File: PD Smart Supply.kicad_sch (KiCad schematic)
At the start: 0 parts

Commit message: Added some major parts to the sheet
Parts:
- added U1: CH224A, easyeda2kicad:ESSOP-10_L4.9-W3.9-P1.0-LS6.0-TL-EP, symbol PD Smart Supply:CH224A
- added U2: TPS560430XDBVR, easyeda2kicad:SOT-23-6_L2.9-W1.6-P0.95-LS2.8-BL, symbol PD Smart Supply:TPS560430XDBVR
- added U3: STM32G071CBT6, easyeda2kicad:LQFP-48_L7.0-W7.0-P0.50-LS9.0-BL, symbol PD Smart Supply:STM32G071CBT6
- added USB1: USB4105-GF-A-060, easyeda2kicad:USB-C-SMD_GT-USB-7010E-1, symbol PD Smart Supply:USB4105-GF-A-060
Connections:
- new net: USB1.A4B9 (VBUS), USB1.B4A9 (VBUS)
- new net: U1.4 (DP), USB1.A6 (DP1), USB1.B6 (DP2)
- new net: U1.5 (DM), USB1.A7 (DN1), USB1.B7 (DN2)
- new net CC1: USB1.A5 (CC1)
- new net CC2: USB1.B5 (CC2)
- new net GND: USB1.1 (GND), USB1.2 (GND), USB1.3 (GND), USB1.4 (GND), USB1.A1B12 (GND), USB1.B1A12 (GND)
- no-connect marks 0 -> 2

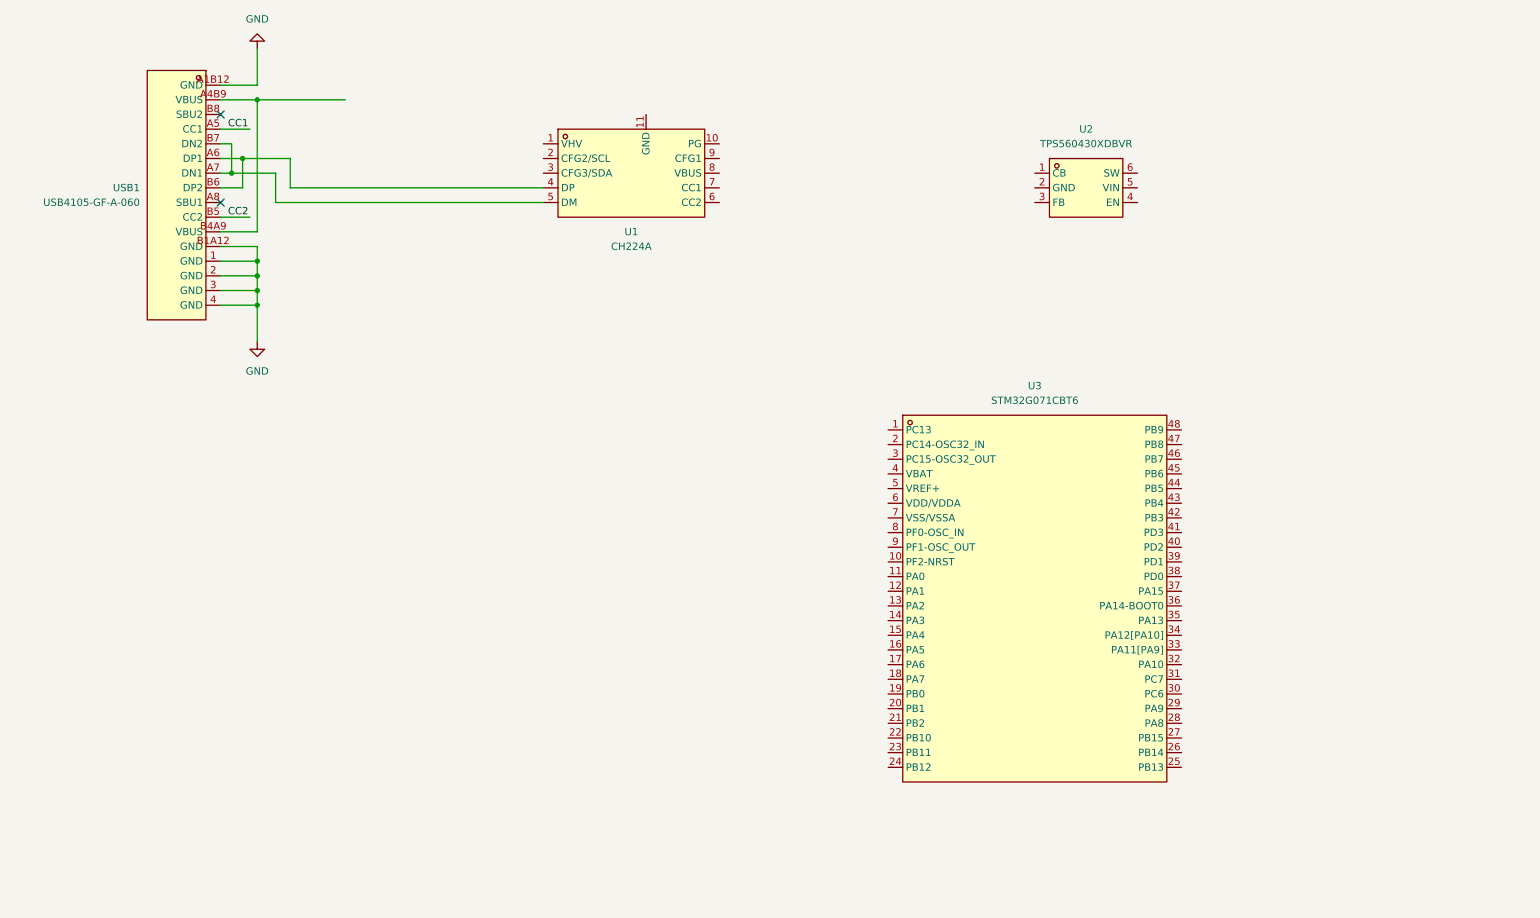
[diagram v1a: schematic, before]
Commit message: Finished schematic work for USB C, pd chip, board 3v3 regulator and added the mcu
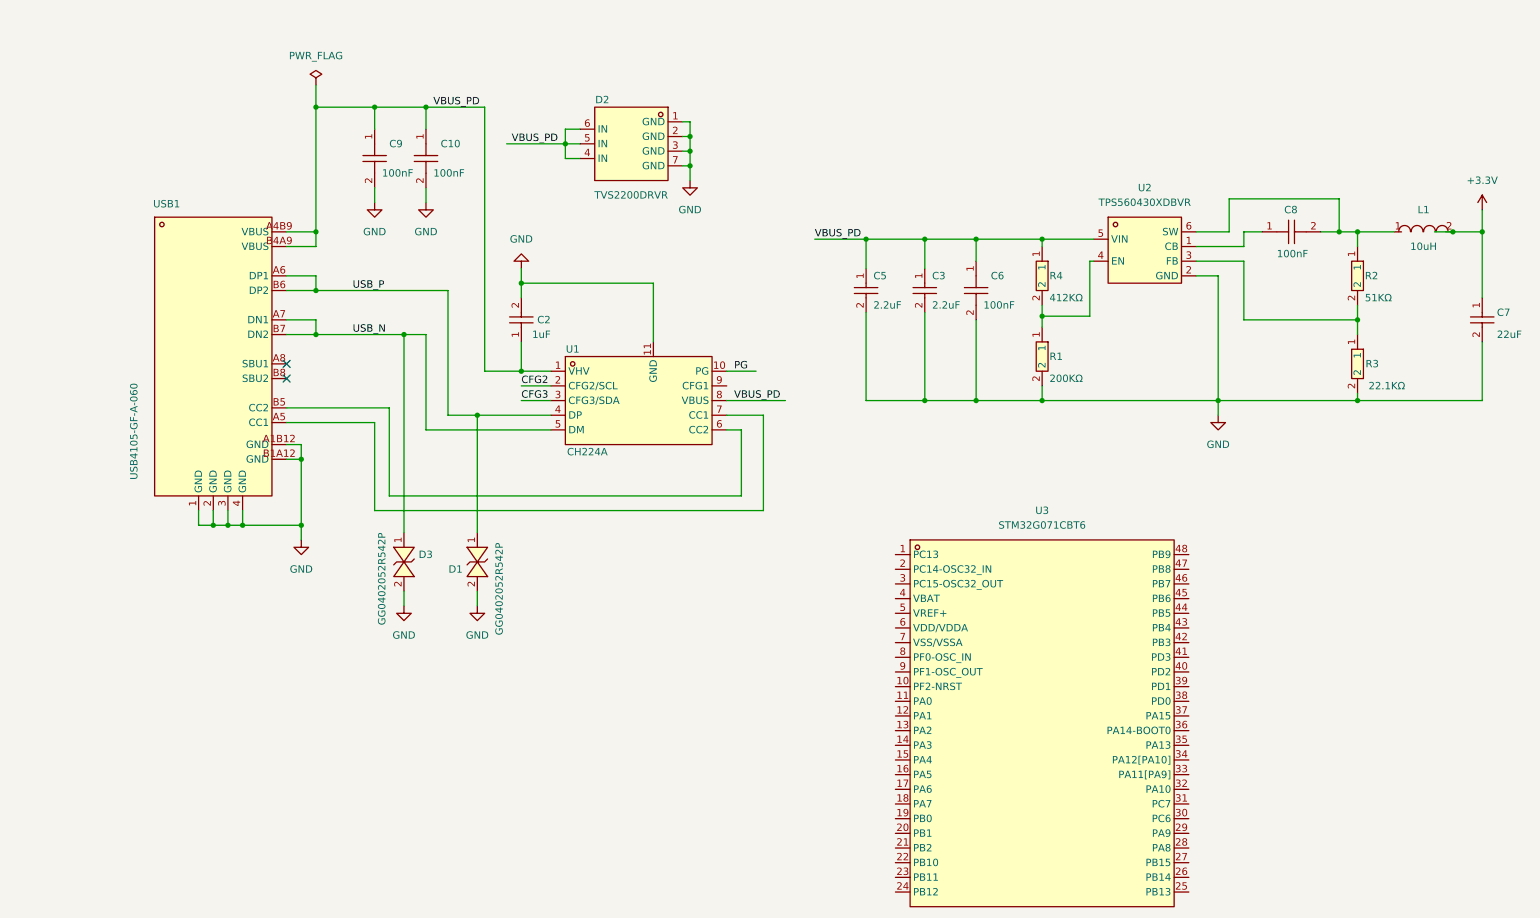
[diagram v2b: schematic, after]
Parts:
- added C10, C6, C8, C9: 100nF, easyeda2kicad:C0603, symbol PD Smart Supply:CC0603KRX7R9BB104
- added C2: 1uF, easyeda2kicad:C0805, symbol PD Smart Supply:CL21B105KBFNNNE
- added C3, C5: 2.2uF, easyeda2kicad:C1206, symbol PD Smart Supply:CL31B225KBHNNNE
- added C7: 22uF, easyeda2kicad:C1206, symbol PD Smart Supply:1206B226K100NT
- added D1, D3: GG0402052R542P, easyeda2kicad:D0402-BI, symbol PD Smart Supply:GG0402052R542P
- added D2: TVS2200DRVR, easyeda2kicad:WSON-6_L2.0-W2.0-P0.65-BL-EP, symbol PD Smart Supply:TVS2200DRVR
- added L1: 10uH, easyeda2kicad:IND-SMD_L5.0-W5.0_FNR50XXS, symbol PD Smart Supply:FNR5040S100MT
- added R1: 200KΩ, easyeda2kicad:R0603, symbol PD Smart Supply:RS-03K2003FT
- added R2: 51KΩ, easyeda2kicad:R0603, symbol PD Smart Supply:0603WAF5102T5E
- added R3: 22.1KΩ, easyeda2kicad:R0603, symbol PD Smart Supply:RC0603FR-0722K1L
- added R4: 412KΩ, easyeda2kicad:R0603, symbol PD Smart Supply:0603WAF4123T5E
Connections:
- net CC1 is gone; now on an unnamed net: USB1.A5 (CC1)
- net CC2 is gone; now on an unnamed net: USB1.B5 (CC2)
- net GND: now also U1.11 (GND), U2.2 (GND), C10.2, C2.2, C3.2, C5.2, C6.2, C7.2, C9.2, D1.2, D2.1 (GND), D2.2 (GND), D2.3 (GND), D2.7 (GND), D3.2, R1.2, R3.2
- net VBUS_PD: now reaches USB1.A4B9 (VBUS), USB1.B4A9 (VBUS)
- net VBUS_PD: now also U1.1 (VHV), U1.8 (VBUS), U2.5 (VIN), C10.1, C2.1, C3.1, C5.1, C6.1, C9.1, D2.4 (IN), D2.5 (IN), D2.6 (IN), R4.1
- net USB_P: now reaches U1.4 (DP), USB1.A6 (DP1), USB1.B6 (DP2)
- net USB_P: now also D1.1
- net USB_N: now reaches U1.5 (DM), USB1.A7 (DN1), USB1.B7 (DN2)
- net USB_N: now also D3.1
- net at U2.1 (CB): now also C8.1
- net at U2.3 (FB): now also R2.2, R3.1
- net at U2.4 (EN): now also R1.1, R4.2
- net at U2.6 (SW): now also C8.2, L1.1, R2.1
- net PG: now reaches U1.10 (PG)
- net CFG2: now reaches U1.2 (CFG2/SCL)
- net CFG3: now reaches U1.3 (CFG3/SDA)
- new net +3.3V: C7.1, L1.2
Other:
- moved on the sheet: U1, U3, USB1

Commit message: Complete Rev A schematic with sensing and test points
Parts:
- added C1, C12, C13, C17, C4: 100nF, PD Smart Supply:C0603, symbol PD Smart Supply:CC0603KRX7R9BB104
- added C11: 4.7uF, PD Smart Supply:C0603, symbol PD Smart Supply:CL21A475KAQNNNE
- added C14: 1uF, PD Smart Supply:C0805, symbol PD Smart Supply:CL21B105KBFNNNE
- added C15: 10uF, PD Smart Supply:C1210, symbol PD Smart Supply:CL32B106KBJNFNE
- added C16: 2.2nF, PD Smart Supply:C0805, symbol PD Smart Supply:CL21C222JBFNNNE
- added D4: SS34, PD Smart Supply:SMA_L4.3-W2.6-LS5.2-RD, symbol PD Smart Supply:SS34_C8678
- added H1: 61300411121, PD Smart Supply:HDR-TH_4P-P2.54-V-M-1, symbol PD Smart Supply:61300411121
- added LED1: KT-0603R, PD Smart Supply:LED-SMD_L1.6-W0.8-R-RD, symbol PD Smart Supply:KT-0603R
- added P1, P2: WJ500V-5.08-2P-14-00A, PD Smart Supply:CONN-TH_2P-P5.00_WJ500V-5.08-2P, symbol PD Smart Supply:WJ500V-5.08-2P-14-00A
- added Q1, Q2: 2N7002, PD Smart Supply:SOT-23-3_L2.9-W1.3-P1.90-LS2.4-BR, symbol PD Smart Supply:2N7002
- added R10, R9: 4.7KΩ, PD Smart Supply:R0402, symbol PD Smart Supply:0402WGF4701TCE
- added R11: 2.2MΩ, PD Smart Supply:R0603, symbol PD Smart Supply:0603WAF2204T5E
- added R12, R23, R24, R25, R8: 1KΩ, PD Smart Supply:R0402, symbol PD Smart Supply:0402WGF1001TCE
- added R13: 100KΩ, PD Smart Supply:R0402, symbol PD Smart Supply:0402WGF1003TCE
- added R14: 820KΩ, PD Smart Supply:R0603, symbol PD Smart Supply:0603WAF8203T5E
- added R15: 887Ω, PD Smart Supply:R0603, symbol PD Smart Supply:0603WAF8870T5E
- added R16, R19, R22, R5, R6, R7: 10KΩ, PD Smart Supply:R0402, symbol PD Smart Supply:0402WGF1002TCE
- added R17, R18, R20, R21: 49.9KΩ, PD Smart Supply:R0603, symbol PD Smart Supply:RC0603FR-0749K9L
- added SW1: Switch, PD Smart Supply:SW-SMD_XYECONN_TSC01-TBW0FH3.5, symbol PD Smart Supply:TSC01-TBW0FH3.5
- added SW2: Rotary Encoder, PD Smart Supply:SW-SMD_EC11J1525402, symbol PD Smart Supply:EC11J1525402
- added TP_3V3: TestPoint, PD Smart Supply:D0402-BI, symbol Connector:TestPoint
- added TP_GND1, TP_ISENSE1, TP_VBUS_PD1, TP_VOUT1, TP_VSENSE1: TestPoint, TestPoint:TestPoint_Pad_D1.5mm, symbol Connector:TestPoint
- added U4: TPS259470LRPWR, PD Smart Supply:VQFN-10_L2.0-W2.0-P0.45-TL, symbol PD Smart Supply:TPS259470LRPWR
- added U5: OLED, PD Smart Supply:OLED-TH_L27.8-W27.2-P2.54_C9900033791, symbol PD Smart Supply:HS96L03W2C03
- C10, C6, C8, C9: footprint easyeda2kicad:C0603 -> PD Smart Supply:C0603
- C2: footprint easyeda2kicad:C0805 -> PD Smart Supply:C0805
- C3, C5, C7: footprint easyeda2kicad:C1206 -> PD Smart Supply:C1206
- D1, D3: footprint easyeda2kicad:D0402-BI -> PD Smart Supply:D0402-BI
- D2: footprint easyeda2kicad:WSON-6_L2.0-W2.0-P0.65-BL-EP -> PD Smart Supply:WSON-6_L2.0-W2.0-P0.65-BL-EP
- L1: footprint easyeda2kicad:IND-SMD_L5.0-W5.0_FNR50XXS -> PD Smart Supply:IND-SMD_L5.0-W5.0_FNR50XXS
- R1, R2, R3, R4: footprint easyeda2kicad:R0603 -> PD Smart Supply:R0603
- U1: footprint easyeda2kicad:ESSOP-10_L4.9-W3.9-P1.0-LS6.0-TL-EP -> PD Smart Supply:ESSOP-10_L4.9-W3.9-P1.0-LS6.0-TL-EP
- U2: footprint easyeda2kicad:SOT-23-6_L2.9-W1.6-P0.95-LS2.8-BL -> PD Smart Supply:SOT-23-6_L2.9-W1.6-P0.95-LS2.8-BL
- U3: footprint easyeda2kicad:LQFP-48_L7.0-W7.0-P0.50-LS9.0-BL -> PD Smart Supply:LQFP-48_L7.0-W7.0-P0.50-LS9.0-BL
- USB1: footprint easyeda2kicad:USB-C-SMD_GT-USB-7010E-1 -> PD Smart Supply:USB-C-SMD_GT-USB-7010E-1
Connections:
- net +3.3V: now also R2.1, U3.4 (VBAT), U3.5 (VREF+), U3.6 (VDD/VDDA), C1.1, C11.1, C13.1, C4.1, R10.1, R13.1, R16.1, R19.2, R23.1, R24.1, R25.1, R5.1, R6.1, R7.1, R8.1, R9.1, TP_3V3.1, U5.2 (VCC)
- net CFG2: now also U3.31 (PC7)
- net CFG3: now also U3.28 (PA8)
- net GND: now also U3.7 (VSS/VSSA), C1.2, C11.2, C12.2, C13.2, C14.2, C15.2, C16.2, C17.2, C4.2, D4.2, H1.2, P1.2, P2.2, Q1.2, Q2.2, R15.2, R18.2, R22.2, SW1.2, SW1.3, SW2.B, SW2.E, TP_GND1.1, U4.8 (GND), U5.1 (GND)
- net PG: now also U3.37 (PA15), Q1.1, R6.2
- net VBUS_PD: now also C14.1, R11.1, R14.1, TP_VBUS_PD1.1, U4.5 (IN)
- net at USB1.A5 (CC1): now also U1.6 (CC2); no longer U1.7 (CC1)
- net at USB1.B5 (CC2): now also U1.7 (CC1); no longer U1.6 (CC2)
- net at C8.2, L1.1, U2.6 (SW): no longer R2.1
- net NRST: now reaches U3.10 (PF2-NRST)
- net NRST: now also C12.1, H1.3, R5.2, SW1.1
- net VOUT_SENSE: now reaches U3.11 (PA0)
- net VOUT_SENSE: now also C17.1, R21.2, R22.1, TP_VSENSE1.1
- net IOUT_SENSE: now reaches U3.12 (PA1)
- net IOUT_SENSE: now also R15.1, TP_ISENSE1.1, U4.9 (ILM)
- net ENC_A: now reaches U3.17 (PA6)
- net ENC_A: now also R23.2, SW2.A
- net ENC_B: now reaches U3.18 (PA7)
- net ENC_B: now also R24.2, SW2.C
- net ENC_SW: now reaches U3.19 (PB0)
- net ENC_SW: now also R25.2, SW2.D
- net EFUSE_OFF: now reaches U3.25 (PB13)
- net EFUSE_OFF: now also R12.1
- net EFUSE_READY: now reaches U3.26 (PB14)
- net EFUSE_READY: now also R16.2, U4.3 (PG/AUXOFF)
- net EFUSE_nFLT: now reaches U3.27 (PB15)
- net EFUSE_nFLT: now also R19.1, U4.4 (~{FLT}/PGTH)
- net CFG1: now reaches U3.30 (PC6)
- net CFG1: now also U1.9 (CFG1), R7.2
- net SWDIO: now reaches U3.35 (PA13)
- net SWDIO: now also H1.1
- net SWCLK: now reaches U3.36 (PA14-BOOT0)
- net SWCLK: now also H1.4
- net OLED_SCL: now reaches U3.45 (PB6)
- net OLED_SCL: now also R10.2, U5.3 (SCL)
- net OLED_SDA: now reaches U3.46 (PB7)
- net OLED_SDA: now also R9.2, U5.4 (SDA)
- new net: R14.2, R17.1
- new net: Q2.1, R12.2, R13.2
- new net: R20.2, R21.1
- new net: LED1.1, R8.2
- new net: LED1.2, Q1.3
- new net: C16.1, U4.7 (DVDT)
- new net EFUSE_OUT: C15.1, D4.1, P1.1, P2.1, R20.1, TP_VOUT1.1, U4.6 (OUT)
- new net EN/UVLO: Q2.3, R11.2, U4.1 (EN/UVLO)
- new net OVLO: R17.2, R18.1, U4.2 (OVLO/OVCSEL)
- no-connect marks 2 -> 36
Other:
- note added: "3V3 Rail"
- note added: "ERROR LED"
- note added: "MCU"
- note added: "OLED Display"
- note added: "OUTPUT eFUSE & MONITORING"
- note added: "Output Connector"
- note added: "Rotary Encoder"
- note added: "SWD Header"
- note added: "USB C, PD and Protection"
- note added: "Voltage Sensing"
- moved on the sheet: C10, C2, C3, C5, C6, C7, C8, C9, D1, D2, D3, L1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

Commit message: Complete Rev A PCB layout and manufacturing preparation
Finalize the four-layer placement, routing, ground pours, silkscreen branding, connector labels, and test-point markings.

Add board design rules, fabrication toolkit settings, project documentation, and ignore regenerable plugin outputs.
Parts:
- removed R23, R24, R25: 1KΩ, PD Smart Supply:R0402, symbol PD Smart Supply:0402WGF1001TCE
- removed SW2: Rotary Encoder, PD Smart Supply:SW-SMD_EC11J1525402, symbol PD Smart Supply:EC11J1525402
- added R26, R27, R28: 10KΩ, PD Smart Supply:R0402, symbol PD Smart Supply:0402WGF1002TCE
- added SW2: Down, PD Smart Supply:SW-SMD_XYECONN_TSC01-TBW0FH3.5, symbol PD Smart Supply:TSC01-TBW0FH3.5
- added SW3: UP, PD Smart Supply:SW-SMD_XYECONN_TSC01-TBW0FH3.5, symbol PD Smart Supply:TSC01-TBW0FH3.5
- added SW4: Select, PD Smart Supply:SW-SMD_XYECONN_TSC01-TBW0FH3.5, symbol PD Smart Supply:TSC01-TBW0FH3.5
- TP_3V3: footprint PD Smart Supply:D0402-BI -> TestPoint:TestPoint_Pad_D1.0mm; now left out of the parts list
- TP_GND1, TP_ISENSE1, TP_VBUS_PD1, TP_VOUT1, TP_VSENSE1: footprint TestPoint:TestPoint_Pad_D1.5mm -> TestPoint:TestPoint_Pad_D1.0mm; now left out of the parts list
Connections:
- net +3.3V: now also R26.1, R27.1, R28.1
- net GND: now also SW2.2, SW2.3, SW3.2, SW3.3, SW4.2, SW4.3
- net at USB1.A5 (CC1): now also U1.7 (CC1); no longer U1.6 (CC2)
- net at USB1.B5 (CC2): now also U1.6 (CC2); no longer U1.7 (CC1)
- net BUCK_SW: now reaches C8.2, L1.1, U2.6 (SW)
- net ENC_A renamed BTN_UP
- net BTN_UP: now also R26.2, SW3.1
- net ENC_B renamed BTN_DOWN
- net BTN_DOWN: now also R27.2, SW2.1
- net ENC_SW renamed BTN_SELECT
- net BTN_SELECT: now also R28.2, SW4.1
- no-connect marks 36 -> 30
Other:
- note added: "CONTROLS"
- note removed: "Rotary Encoder"
- moved on the sheet: C10, C9, LED1, Q1, R8, TP_GND1

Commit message: Finalize Rev A design for manufacturing
Synchronize final component metadata and fabrication settings, preserve the completed PCB state, add the Rev A design record, and organize simulation and calculator references under Docs.
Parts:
- SW1: value Switch -> TSC01-TBW0FH3.5
- SW2: value Down -> TSC01-TBW0FH3.5
- SW3: value UP -> TSC01-TBW0FH3.5
- SW4: value Select -> TSC01-TBW0FH3.5
- U5: value OLED -> HS96L03W2C03
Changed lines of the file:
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@@
 			)
 		)
-		(property "Value" "OLED"
+		(property "Value" "HS96L03W2C03"
 			(at 339.09 224.79 0)
 			(effects
@@
 			)
 		)
-		(property "Value" "UP"
+		(property "Value" "TSC01-TBW0FH3.5"
 			(at 92.71 260.35 0)
 			(effects
@@
 			)
 		)
-		(property "Value" "Select"
+		(property "Value" "TSC01-TBW0FH3.5"
 			(at 190.5 260.35 0)
 			(effects
@@
 			)
 		)
-		(property "Value" "Switch"
+		(property "Value" "TSC01-TBW0FH3.5"
 			(at 182.88 199.39 0)
 			(effects
@@
 			)
 		)
-		(property "Value" "Down"
+		(property "Value" "TSC01-TBW0FH3.5"
 			(at 137.16 260.35 0)
 			(effects
